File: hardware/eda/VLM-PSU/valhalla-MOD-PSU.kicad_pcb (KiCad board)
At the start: 2 copper layers, 76.2 x 50.8 mm, 31 parts, among them J1 MAINS, J2 DC, J3 BUS, J4 GPIO, Q1 *3, U1 *2

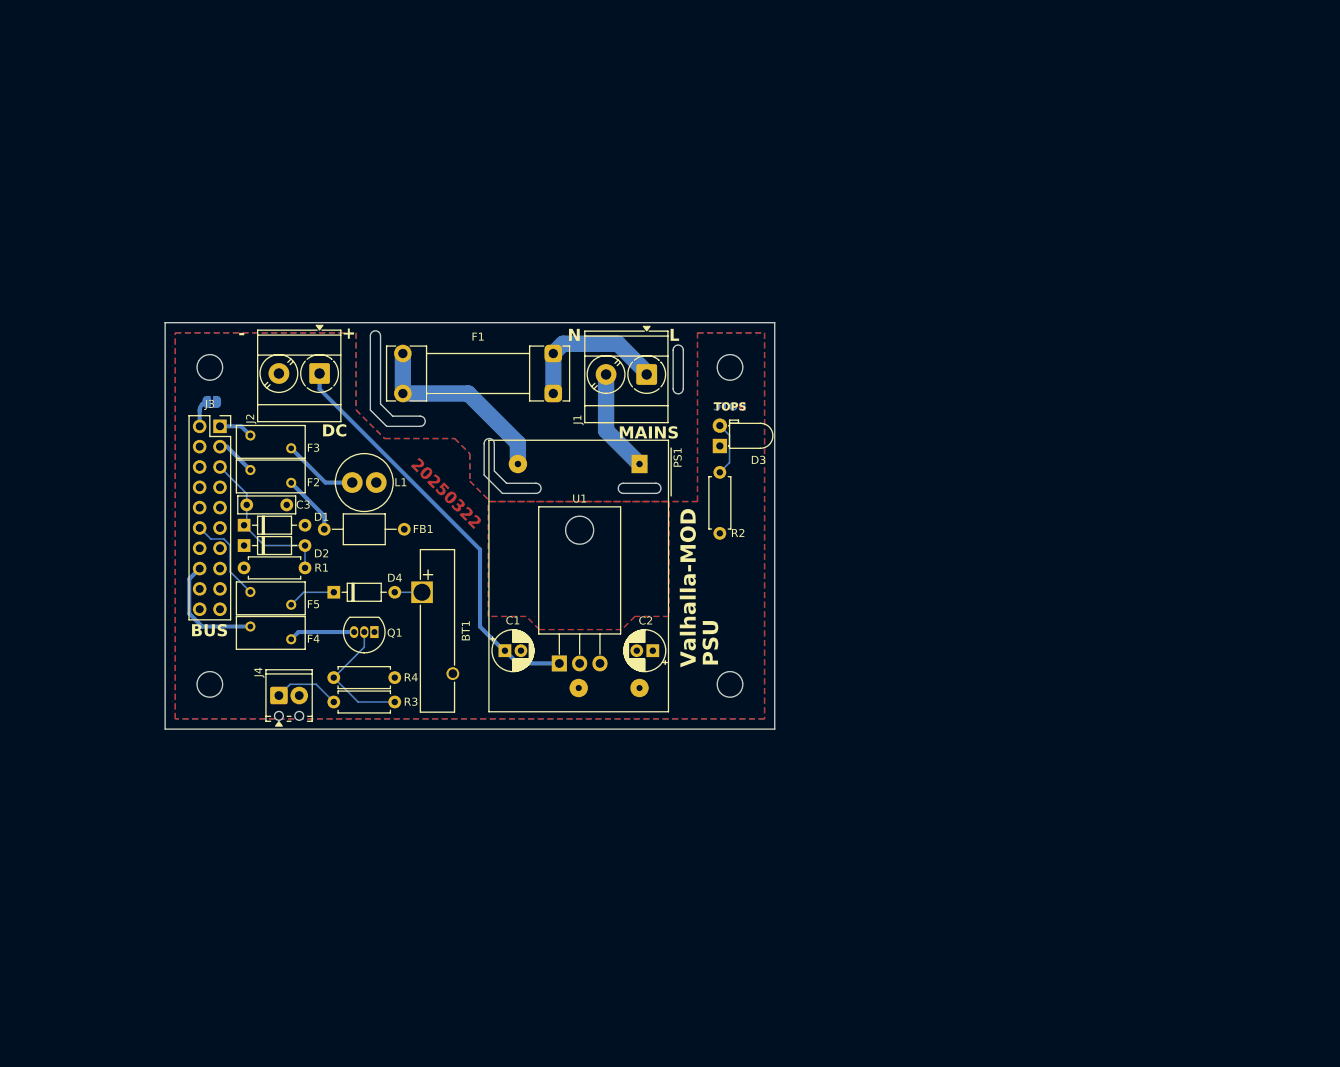
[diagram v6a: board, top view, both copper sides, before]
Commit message: UPDATE: progress on MOD-PSU
 - refined the schematic design and started work on the PCB layout
 - selected some critical components, resolved final footprints
   for others
 - found a good compromise for the (initially) /RESET line: using a
   supervisory circuit BUT using it as a POWER_GOOD output. A
   connected CPU can thus choose whether to interpret that as PG
   (early warning) or /RESET (closing shop).
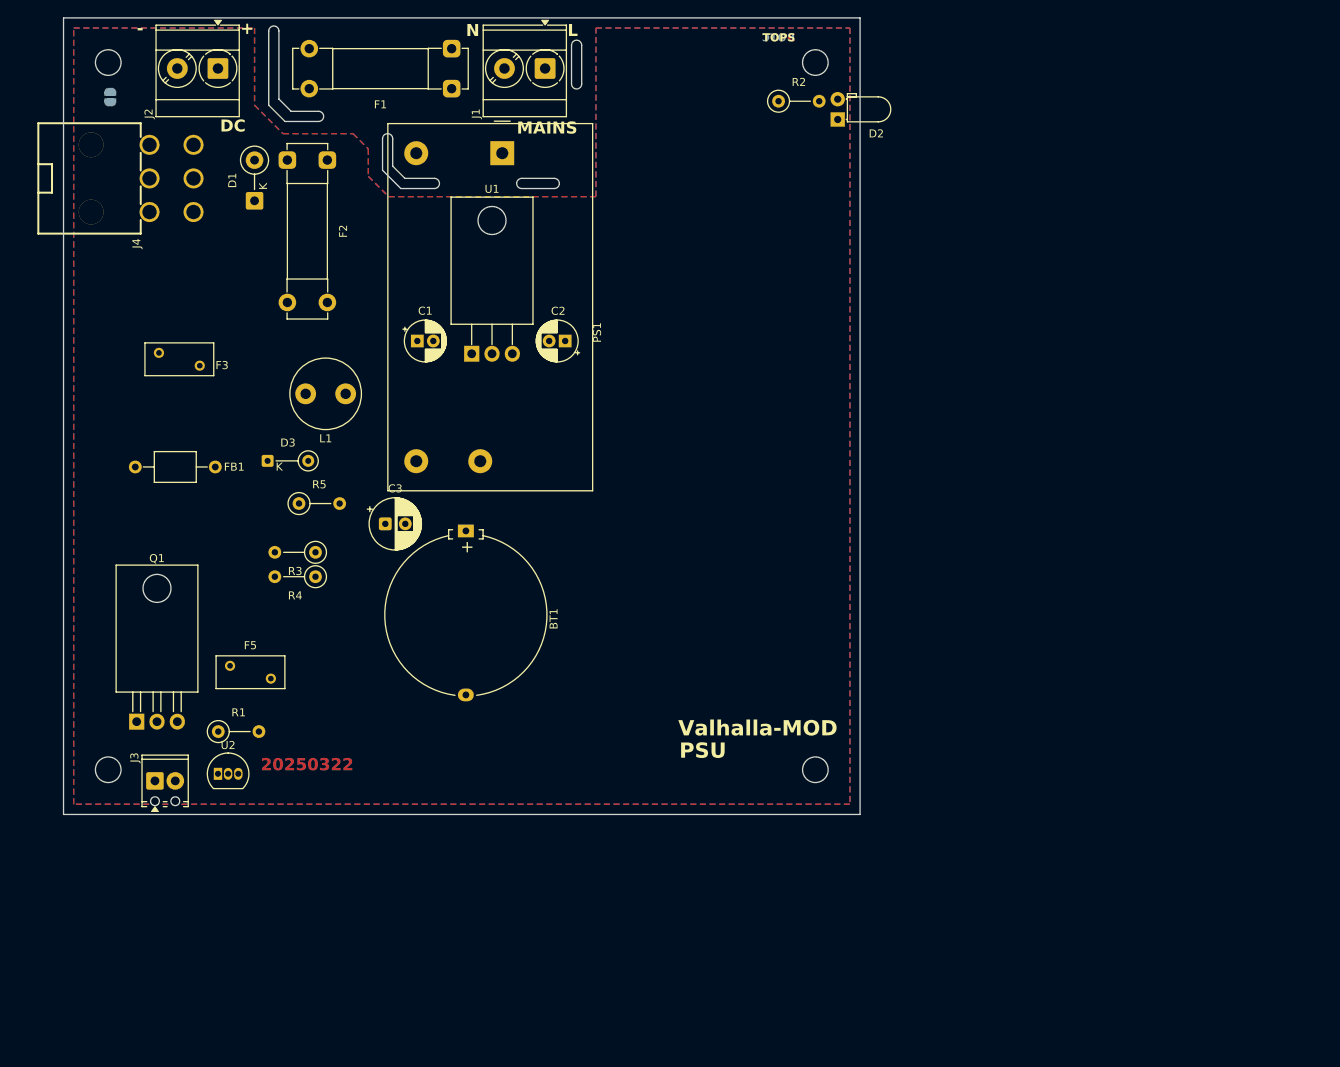
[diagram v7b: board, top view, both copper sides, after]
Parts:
- removed the D2 at (48.0, 91.4)
- removed F4: *3, Fuse:Fuse_BelFuse_0ZRE0005FF_L8.3mm_W3.8mm
- removed the J3 at (45.0, 76.5)
- added J4: POWER, PCM_EasyEDA:CONN-TN_39301060, F.Cu at (38.9, 45.5)
- added R5: 200R, Resistor_THT:R_Axial_DIN0207_L6.3mm_D2.5mm_P5.08mm_Vertical, F.Cu at (54.8, 86.1)
- added U2: MCP111-450E/TO, Package_TO_SOT_THT:TO-92_Inline, F.Cu at (44.7, 119.9)
- BT1: footprint Battery:Battery_Panasonic_CR2032-VS1N_Vertical_CircularHoles -> Battery:Battery_Panasonic_CR2032-HFN_Horizontal_CircularHoles
- C1: value *3 -> 10uF/63V
- C2: value *3 -> 22uF/16V
- C3: value 4.7nF -> 220uF/16V; footprint Capacitor_THT:C_Rect_L7.0mm_W2.0mm_P5.00mm -> Capacitor_THT:CP_Radial_D6.3mm_P2.50mm
- D1: value 5V -> 36V; footprint Diode_THT:D_DO-35_SOD27_P7.62mm_Horizontal -> Diode_THT:D_DO-41_SOD81_P5.08mm_Vertical_KathodeUp
- D3: renamed from D4; value BAT54 -> BAT43; footprint Diode_THT:D_DO-35_SOD27_P7.62mm_Horizontal -> Diode_THT:D_DO-34_SOD68_P5.08mm_Vertical_KathodeUp
- F1: value *1 -> T2AL 300V; footprint Fuse:Fuseholder_Clip-5x20mm_Littelfuse_111_Lateral_P18.80x5.00mm_D1.17mm_Horizontal -> Fuse:Fuseholder_Clip-5x20mm_Bel_FC-203-22_Lateral_P17.80x5.00mm_D1.17mm_Horizontal
- F2: value *1 -> T1.5AL 250V; footprint Fuse:Fuse_BelFuse_0ZRE0005FF_L8.3mm_W3.8mm -> Fuse:Fuseholder_Clip-5x20mm_Bel_FC-203-22_Lateral_P17.80x5.00mm_D1.17mm_Horizontal
- F5: value 25mA -> 500mA
- L1: footprint Inductor_THT:L_Radial_D7.0mm_P3.00mm -> Inductor_THT:L_Radial_D8.7mm_P5.00mm_Fastron_07HCP
- PS1: value IRM-02-*2 -> IRM-05/10-5; footprint Converter_ACDC:Converter_ACDC_MeanWell_IRM-02-xx_THT -> Converter_ACDC:Converter_ACDC_MeanWell_IRM-05-xx_THT
- Q1: value *3 -> IRF9Z34N; footprint Package_TO_SOT_THT:TO-92_Inline -> Package_TO_SOT_THT:TO-220-3_Horizontal_TabDown
- R1: value 47K -> 10K; footprint Resistor_THT:R_Axial_DIN0207_L6.3mm_D2.5mm_P7.62mm_Horizontal -> Resistor_THT:R_Axial_DIN0207_L6.3mm_D2.5mm_P5.08mm_Vertical
- R2: value *4 -> 820R; footprint Resistor_THT:R_Axial_DIN0207_L6.3mm_D2.5mm_P7.62mm_Horizontal -> Resistor_THT:R_Axial_DIN0207_L6.3mm_D2.5mm_P5.08mm_Vertical
- R3: renamed from R4; footprint Resistor_THT:R_Axial_DIN0207_L6.3mm_D2.5mm_P7.62mm_Horizontal -> Resistor_THT:R_Axial_DIN0207_L6.3mm_D2.5mm_P5.08mm_Vertical
- R4: renamed from R3; value 2K2 -> 470R; footprint Resistor_THT:R_Axial_DIN0207_L6.3mm_D2.5mm_P7.62mm_Horizontal -> Resistor_THT:R_Axial_DIN0207_L6.3mm_D2.5mm_P5.08mm_Vertical
- U1: value *2 -> N7805-1P
- moved R2 54.5 mm to (114.8, 35.8), turned to 0 degrees
- moved D2 43.4 mm to (122.2, 38.1)
- moved PS1 42.5 mm to (80.2, 42.3)
- moved F2 40.6 mm to (58.4, 43.2), turned to -90 degrees
- moved D1 40.6 mm to (49.3, 48.3), turned to 90 degrees
- moved J1 40.3 mm to (85.6, 31.7)
- moved C2 40.2 mm to (88.1, 65.8)
- moved U1 40.2 mm to (76.4, 67.4)
- moved C1 40.2 mm to (69.6, 65.8)
- moved J2 40.2 mm to (44.7, 31.7)
- moved JP1 40.2 mm to (31.2, 35.3), turned to -90 degrees
- moved F1 40.2 mm to (73.9, 34.2)
- moved H1 40.2 mm to (31.0, 31.0)
- moved H3 39.6 mm to (119.4, 31.0)
- moved Q1 31.8 mm to (34.5, 113.4), turned to 0 degrees
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- renumbered D3 to D2, J4 to J3
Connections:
- C1 pad 1: Net-(J2-Pin_1) -> Net-(D1-K)
- C2 pad 1: Net-(D2-K) -> Net-(PS1-+Vo)
- C3 pad 1: /~{RESET} -> Net-(PS1-+Vo)
- D1 pad 1: /~{RESET} -> Net-(D1-K)
- D3 pad 1: Net-(D4-K) -> /BVCC
- D3 pad 2: Net-(BT1-+) -> Net-(D3-A)
- F1 pad 1: Net-(J1-Pin_1) -> Net-(J1-Pin_2)
- F2 pad 1: Net-(F2-Pad1) -> Net-(J2-Pin_1)
- F2 pad 2: /DVCC -> Net-(D1-K)
- F5 pad 1: Net-(D4-K) -> Net-(Q1-D)
- F5 pad 2: /BVCC -> /LVCC
- FB1 pad 1: Net-(D2-K) -> Net-(PS1-+Vo)
- FB1 pad 2: Net-(F2-Pad1) -> /DVCC
- J3 pad 1: /ILLUMINATION -> /POWER_GOOD
- J3 pad 2: unconnected-(J4-Pin_2-Pad2) -> /~{ILLUMINATION}
- L1 pad 1: Net-(D2-K) -> Net-(PS1-+Vo)
- PS1 pad 1: Net-(J1-Pin_2) -> Net-(J1-Pin_1)
- PS1 pad 4: Net-(D2-K) -> Net-(PS1-+Vo)
- Q1 pad 1: Net-(D2-K) -> Net-(Q1-G)
- Q1 pad 2: Net-(Q1-G) -> Net-(Q1-D)
- Q1 pad 3: Net-(Q1-S) -> Net-(PS1-+Vo)
- R1 pad 1: Net-(D2-K) -> Net-(PS1-+Vo)
- R1 pad 2: /~{RESET} -> /POWER_GOOD
- R2 pad 1: Net-(D2-K) -> Net-(PS1-+Vo)
- R3 pad 1: Net-(D2-K) -> Net-(PS1-+Vo)
- R4 pad 2: /ILLUMINATION -> /~{ILLUMINATION}
- U1 pad 1: Net-(J2-Pin_1) -> Net-(D1-K)
- U1 pad 3: Net-(D2-K) -> Net-(PS1-+Vo)
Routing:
- net Net-(J2-Pin_1): track 51.7 -> 0.00 mm
- net Net-(PS1-AC/L): track 24.6 -> 0.00 mm
- net /~{RESET}: track 19.8 -> 0.00 mm
- net Net-(J1-Pin_1): track 18.7 -> 0.00 mm
- net Net-(Q1-G): track 16.2 -> 0.00 mm
- net /LVCC: track 14.5 -> 0.00 mm
- net Net-(J1-Pin_2): track 13.2 -> 0.00 mm
- net /BVCC: track 11.6 -> 0.00 mm
- net Net-(F3-Pad1): track 9.41 -> 0.00 mm
- net /ILLUMINATION: track 8.36 -> 0.00 mm
- net Net-(Q1-S): track 8.24 -> 0.00 mm
- net Net-(F2-Pad1): track 7.52 -> 0.00 mm
- net Net-(D2-A): track 6.84 -> 0.00 mm
- net Net-(D4-K): track 5.97 -> 0.00 mm
- net /DVCC: track 5.01 -> 0.00 mm
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- added copper zone on F.Cu, net Net-(PS1-+Vo)
- removed copper zone on F.Cu, net Net-(D2-K)
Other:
- board size 76.2 x 50.8 mm -> 99.6 x 99.6 mm
- board text removed: "BUS"

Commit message: UPDATE: MOD-PSU revamped schematic should be done
 - allowed for all assembly variants:
  - single AC supply
  - single DC supply
  - dual AC/DC supply with ideal diode OR-ing
 - allowed for remote on/off option for both types of supplies
 - layout is next.
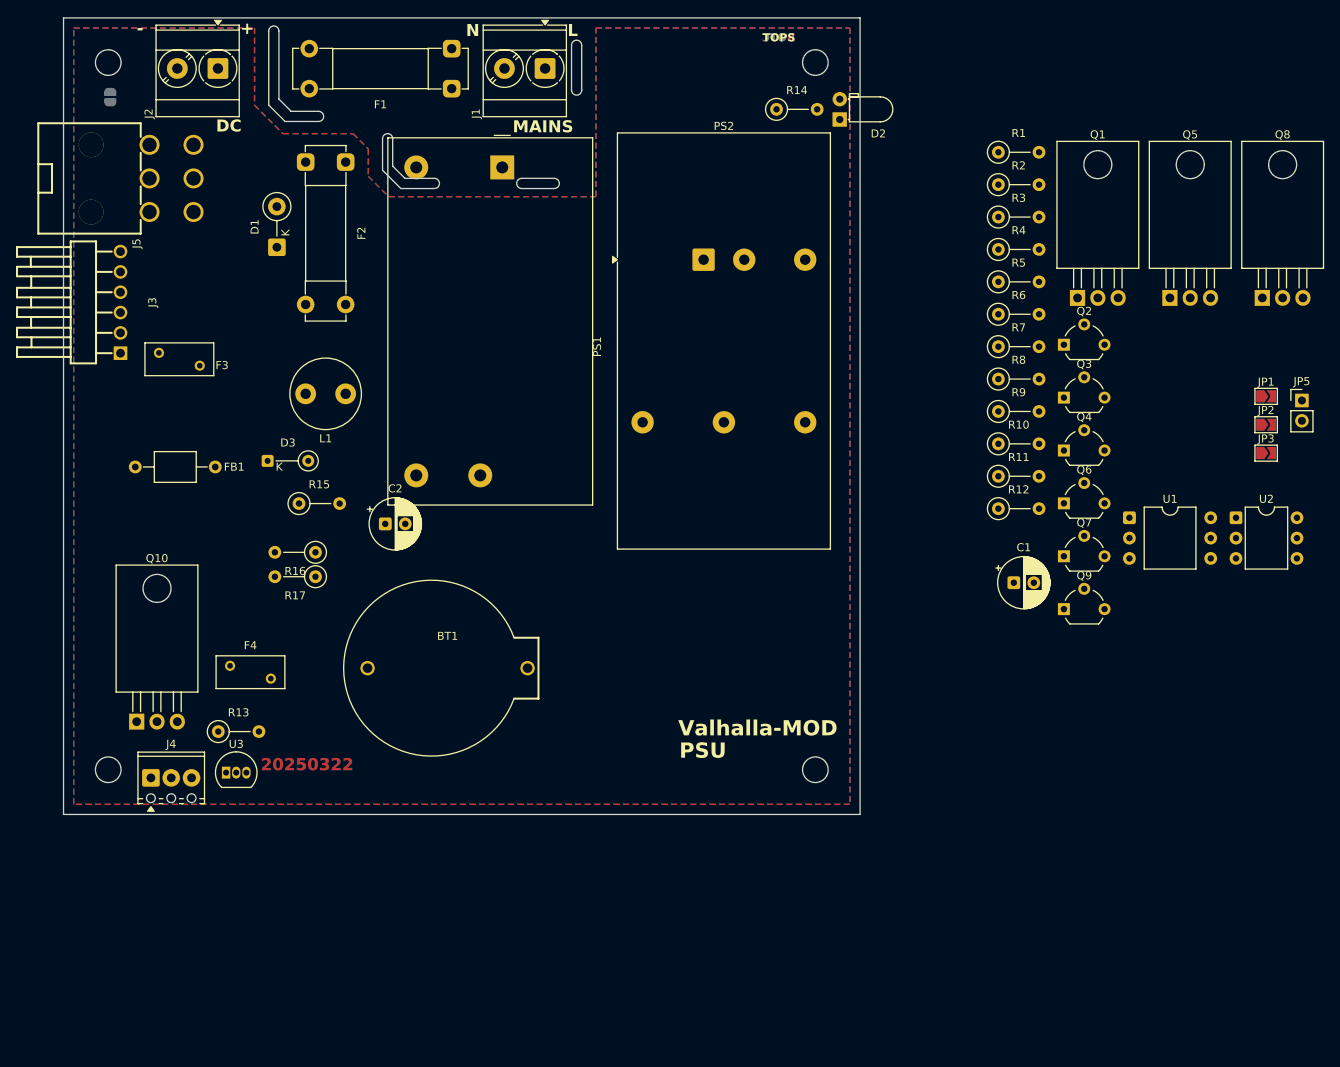
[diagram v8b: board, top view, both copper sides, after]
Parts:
- removed the C2 at (88.1, 65.8)
- added J4: GPIO, TerminalBlock_Phoenix:TerminalBlock_Phoenix_MPT-0,5-3-2.54_1x03_P2.54mm_Horizontal, F.Cu at (36.3, 120.4)
- added JP1: ~{REMOTE}, Jumper:SolderJumper-2_P1.3mm_Open_TrianglePad1.0x1.5mm, F.Cu at (175.7, 72.7)
- added JP2: SINGLE, Jumper:SolderJumper-2_P1.3mm_Open_TrianglePad1.0x1.5mm, F.Cu at (175.7, 76.3)
- added JP3: SINGLE, Jumper:SolderJumper-2_P1.3mm_Open_TrianglePad1.0x1.5mm, F.Cu at (175.7, 79.8)
- added JP5: ILLUMINATION, Connector_PinHeader_2.54mm:PinHeader_1x02_P2.54mm_Vertical, F.Cu at (180.2, 73.2)
- added PS2: NSD10-12S5, Converter_DCDC:Converter_DCDC_MeanWell_NSD10_THT, F.Cu at (105.4, 55.6)
- added Q1: BTA08-600CW, Package_TO_SOT_THT:TO-220-3_Horizontal_TabDown, F.Cu at (152.1, 60.4)
- added Q2: 2N3904, Package_TO_SOT_THT:TO-92_Wide, F.Cu at (150.4, 66.3)
- added Q3: 2N3906, Package_TO_SOT_THT:TO-92_Wide, F.Cu at (150.4, 72.9)
- added Q4: 2N3906, Package_TO_SOT_THT:TO-92_Wide, F.Cu at (150.4, 79.5)
- added Q5: SUP90P06-09L, Package_TO_SOT_THT:TO-220-3_Horizontal_TabDown, F.Cu at (163.7, 60.4)
- added Q6: 2N3906, Package_TO_SOT_THT:TO-92_Wide, F.Cu at (150.4, 86.1)
- added Q7: 2N3906, Package_TO_SOT_THT:TO-92_Wide, F.Cu at (150.4, 92.7)
- added Q8: SUP90P06-09L, Package_TO_SOT_THT:TO-220-3_Horizontal_TabDown, F.Cu at (175.2, 60.4)
- added Q9: 2N3906, Package_TO_SOT_THT:TO-92_Wide, F.Cu at (150.4, 99.3)
- added R1: 360R, Resistor_THT:R_Axial_DIN0207_L6.3mm_D2.5mm_P5.08mm_Vertical, F.Cu at (142.3, 42.2)
- added R10: 10K, Resistor_THT:R_Axial_DIN0207_L6.3mm_D2.5mm_P5.08mm_Vertical, F.Cu at (142.3, 78.6)
- added R11: 10K, Resistor_THT:R_Axial_DIN0207_L6.3mm_D2.5mm_P5.08mm_Vertical, F.Cu at (142.3, 82.7)
- added R12: 10K, Resistor_THT:R_Axial_DIN0207_L6.3mm_D2.5mm_P5.08mm_Vertical, F.Cu at (142.3, 86.7)
- added R2: 360R, Resistor_THT:R_Axial_DIN0207_L6.3mm_D2.5mm_P5.08mm_Vertical, F.Cu at (142.3, 46.2)
- added R3: 820R, Resistor_THT:R_Axial_DIN0207_L6.3mm_D2.5mm_P5.08mm_Vertical, F.Cu at (142.3, 50.3)
- added R4: 100K, Resistor_THT:R_Axial_DIN0207_L6.3mm_D2.5mm_P5.08mm_Vertical, F.Cu at (142.3, 54.3)
- added R5: 4K7, Resistor_THT:R_Axial_DIN0207_L6.3mm_D2.5mm_P5.08mm_Vertical, F.Cu at (142.3, 58.4)
- added R6: 750R, Resistor_THT:R_Axial_DIN0207_L6.3mm_D2.5mm_P5.08mm_Vertical, F.Cu at (142.3, 62.4)
- added R7: 10K, Resistor_THT:R_Axial_DIN0207_L6.3mm_D2.5mm_P5.08mm_Vertical, F.Cu at (142.3, 66.5)
- added R8: 4K7, Resistor_THT:R_Axial_DIN0207_L6.3mm_D2.5mm_P5.08mm_Vertical, F.Cu at (142.3, 70.5)
- added R9: 10K, Resistor_THT:R_Axial_DIN0207_L6.3mm_D2.5mm_P5.08mm_Vertical, F.Cu at (142.3, 74.6)
- added U2: 4N35, Package_DIP:DIP-6_W7.62mm, F.Cu at (172.0, 87.9)
- BT1: footprint Battery:Battery_Panasonic_CR2032-HFN_Horizontal_CircularHoles -> PCM_EasyEDA:BAT-TH_BS-02-A1AJ010
- C1: value 10uF/63V -> 220uF/100V; footprint Capacitor_THT:CP_Radial_D5.0mm_P2.00mm -> Capacitor_THT:CP_Radial_D6.3mm_P2.50mm
- F1: value T2AL 300V -> T2AL 250V
- F2: value T1.5AL 250V -> T2AL 250V
- J3: value GPIO -> BUS; footprint TerminalBlock_Phoenix:TerminalBlock_Phoenix_MPT-0,5-2-2.54_1x02_P2.54mm_Horizontal -> PCM_EasyEDA:Molex_KK-254_A-7478-06A_1x06_P2.54mm_Horizontal
- JP4: renamed from JP1; value *5 -> AGND_STAR
- U1: value N7805-1P -> MOC3063M; footprint Package_TO_SOT_THT:TO-220-3_Horizontal_TabDown -> Package_DIP:DIP-6_W10.16mm
- moved U1 84.7 mm to (158.6, 87.9)
- moved C1 80.5 mm to (144.2, 96.0)
- moved J3 60.0 mm to (32.5, 61.0), turned to -90 degrees
- moved BT1 17.3 mm to (73.4, 106.7), turned to 0 degrees
- moved D1 6.44 mm to (52.1, 54.1)
- moved F2 2.30 mm to (60.7, 43.4)
- moved PS1 1.78 mm to (80.2, 44.1)
- moved R14 1.05 mm to (114.5, 36.8)
- moved U3 1.03 mm to (45.7, 119.7)
- moved D2 0.25 mm to (122.4, 38.1)
- renumbered C3 to C2, F5 to F4, J4 to J5, Q1 to Q10, R1 to R13, R2 to R14, R5 to R15, R3 to R16, R4 to R17, U2 to U3
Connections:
- C1 pad 2: /DGND -> Net-(D1-A)
- C2 pad 1: Net-(PS1-+Vo) -> Net-(JP2-B)
- D1 pad 2: /DGND -> Net-(D1-A)
- F1 pad 2: Net-(PS1-AC/L) -> Net-(JP1-A)
- FB1 pad 1: Net-(PS1-+Vo) -> Net-(JP2-B)
- J2 pad 2: /DGND -> Net-(D1-A)
- J3 pad 1: /POWER_GOOD -> unconnected-(J3-Pin_1-Pad1)
- J3 pad 2: /~{ILLUMINATION} -> /BUS_DVCC
- L1 pad 1: Net-(PS1-+Vo) -> Net-(JP2-B)
- PS1 pad 2: Net-(PS1-AC/L) -> Net-(JP1-B)
- PS1 pad 4: Net-(PS1-+Vo) -> Net-(JP2-A)
- Q10 pad 3: Net-(PS1-+Vo) -> Net-(JP2-B)
- R13 pad 1: Net-(PS1-+Vo) -> Net-(JP2-B)
- R13 pad 2: /POWER_GOOD -> /PGOOD/~{RESET}
- R14 pad 1: Net-(PS1-+Vo) -> Net-(JP2-B)
- R16 pad 1: Net-(PS1-+Vo) -> Net-(JP2-B)
- U1 pad 1: Net-(D1-K) -> Net-(R3-Pad1)
- U1 pad 2: /DGND -> Net-(Q2-C)
- U1 pad 3: Net-(PS1-+Vo) -> unconnected-(U1-NC-Pad3)
- U3 pad 1: /POWER_GOOD -> /PGOOD/~{RESET}
- U3 pad 2: Net-(PS1-+Vo) -> Net-(JP2-B)
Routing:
- added copper zone on F.Cu, net Net-(JP2-B)
- removed copper zone on F.Cu, net Net-(PS1-+Vo)
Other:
- outline, holes or cut-outs redrawn
